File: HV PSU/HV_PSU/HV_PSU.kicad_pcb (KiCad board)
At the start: 2 copper layers, 106 parts, among them J1 Screw_Terminal_01x07, J10 MountingHole_Pad, J11 MountingHole_Pad, J12 MountingHole_Pad, J13 MountingHole_Pad, J2 MountingHole_Pad, J3 MountingHole_Pad, J4 MountingHole_Pad, J5 MountingHole_Pad, J6 MountingHole_Pad, J7 MountingHole_Pad, J8 MountingHole_Pad, J9 MountingHole_Pad, Q1 2N7002, Q2 IRFS4227, Q3 IRFS4227, U1 L7812, U2 TPS2814D

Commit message: backup
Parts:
- C10, C11, C12, C13, C6, C7, C8, C9: footprint Capacitor_THT:C_Disc_D16.0mm_W5.0mm_P10.00mm -> HV_caps:HVC-30KV-D17-F12.5-102K
- D1, D2: value UF4007 -> 1N4148WS; footprint Diode_THT:D_DO-41_SOD81_P10.16mm_Horizontal -> Diode_SMD:D_SOD-323
- D20, D21, D22, D23: value UF4007 -> ES1J; footprint Diode_THT:D_DO-41_SOD81_P10.16mm_Horizontal -> Diode_SMD:D_SMA-SMB_Universal_Handsoldering
- moved D4 175.6 mm to (120.5, 156.8)
- moved D5 175.6 mm to (139.7, 152.4)
- moved D7 158.9 mm to (129.5, 180.3)
- moved D6 158.9 mm to (149.1, 170.8)
- moved D8 153.4 mm to (180.0, 170.3), turned to 90 degrees
- moved J2 133.3 mm to (219.7, 87.6)
- moved D9 115.4 mm to (185.4, 170.2), turned to 90 degrees
- moved D15 107.1 mm to (227.3, 168.9), turned to 90 degrees
- moved C8 103.3 mm to (268.1, 85.1)
- moved R11 101.9 mm to (172.7, 129.5)
- moved D10 101.8 mm to (194.3, 170.2), turned to 90 degrees
- moved J4 101.6 mm to (233.7, 180.3)
- moved J3 101.2 mm to (233.7, 147.3)
- moved C10 100.0 mm to (280.8, 91.4)
- moved D13 96.8 mm to (209.6, 171.4), turned to 90 degrees
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
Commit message: Some PCB placement
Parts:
- moved D4 147.6 mm to (254.5, 95.0), turned to -90 degrees
- moved D7 140.2 mm to (264.8, 143.4), turned to 90 degrees
- moved D6 130.0 mm to (264.1, 110.2), turned to 90 degrees
- moved D8 120.2 mm to (273.7, 95.0), turned to -90 degrees
- moved D5 117.5 mm to (254.6, 128.1), turned to -90 degrees
- moved D12 108.8 mm to (292.8, 95.0), turned to -90 degrees
- moved D10 107.3 mm to (283.2, 110.2)
- moved D16 101.9 mm to (312.0, 95.0), turned to -90 degrees
- moved D9 99.0 mm to (275.0, 128.1), turned to -90 degrees
- moved D13 96.2 mm to (295.4, 128.1), turned to -90 degrees
- moved R12 93.8 mm to (265.3, 120.8), turned to 90 degrees
- moved R10 93.1 mm to (265.3, 114.4), turned to 90 degrees
- moved R32 93.0 mm to (313.3, 120.8), turned to 90 degrees
- moved R30 92.8 mm to (313.3, 114.4), turned to 90 degrees
- moved R36 92.0 mm to (322.8, 120.8), turned to 90 degrees
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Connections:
- D10 pad 1: Net-(D10-Pad1) -> Net-(R18-Pad2)
- D10 pad 2: Net-(D10-Pad2) -> Net-(C10-Pad1)
- D11 pad 2: Net-(D10-Pad1) -> Net-(D11-Pad2)
- D12 pad 1: Net-(D12-Pad1) -> Net-(C10-Pad2)
- D12 pad 2: Net-(D12-Pad2) -> Net-(R22-Pad2)
- D13 pad 1: Net-(D12-Pad2) -> Net-(D13-Pad1)
- D14 pad 1: Net-(D14-Pad1) -> Net-(R26-Pad2)
- D14 pad 2: Net-(D14-Pad2) -> Net-(C10-Pad2)
- D15 pad 2: Net-(D14-Pad1) -> Net-(D15-Pad2)
- D16 pad 1: Net-(D16-Pad1) -> Net-(C12-Pad2)
- D17 pad 1: Net-(D16-Pad2) -> Net-(D17-Pad1)
- D18 pad 1: Net-(D18-Pad1) -> Net-(R34-Pad2)
- D18 pad 2: Net-(D18-Pad2) -> Net-(C12-Pad2)
- D19 pad 2: Net-(D18-Pad1) -> Net-(R37-Pad1)
- D4 pad 1: Net-(D4-Pad1) -> Net-(C6-Pad2)
- D4 pad 2: Net-(D4-Pad2) -> Net-(R6-Pad2)
- D5 pad 1: Net-(D4-Pad2) -> Net-(D5-Pad1)
- D6 pad 2: Net-(D6-Pad2) -> Net-(C6-Pad2)
- D7 pad 2: Net-(D6-Pad1) -> Net-(D7-Pad2)
- D8 pad 1: Net-(D8-Pad1) -> Net-(C10-Pad1)
- D8 pad 2: Net-(D8-Pad2) -> Net-(R14-Pad2)
- D9 pad 1: Net-(D8-Pad2) -> Net-(D9-Pad1)
- R10 pad 2: Net-(C6-Pad2) -> Net-(D6-Pad1)
- R13 pad 1: Net-(D6-Pad2) -> Net-(D7-Pad2)
- R14 pad 2: Net-(C10-Pad1) -> Net-(R14-Pad2)
- R17 pad 1: Net-(D8-Pad1) -> Net-(D9-Pad1)
- R18 pad 2: Net-(C10-Pad1) -> Net-(R18-Pad2)
- R21 pad 1: Net-(D10-Pad2) -> Net-(D11-Pad2)
- R22 pad 2: Net-(C10-Pad2) -> Net-(R22-Pad2)
- R25 pad 1: Net-(D12-Pad1) -> Net-(D13-Pad1)
- R26 pad 2: Net-(C10-Pad2) -> Net-(R26-Pad2)
- R29 pad 1: Net-(D14-Pad2) -> Net-(D15-Pad2)
- R30 pad 2: Net-(C12-Pad2) -> Net-(D16-Pad2)
- R33 pad 1: Net-(D16-Pad1) -> Net-(D17-Pad1)
- R34 pad 2: Net-(C12-Pad2) -> Net-(R34-Pad2)
- R37 pad 1: Net-(D18-Pad2) -> Net-(R37-Pad1)
- R6 pad 2: Net-(C6-Pad2) -> Net-(R6-Pad2)
- R9 pad 1: Net-(D4-Pad1) -> Net-(D5-Pad1)

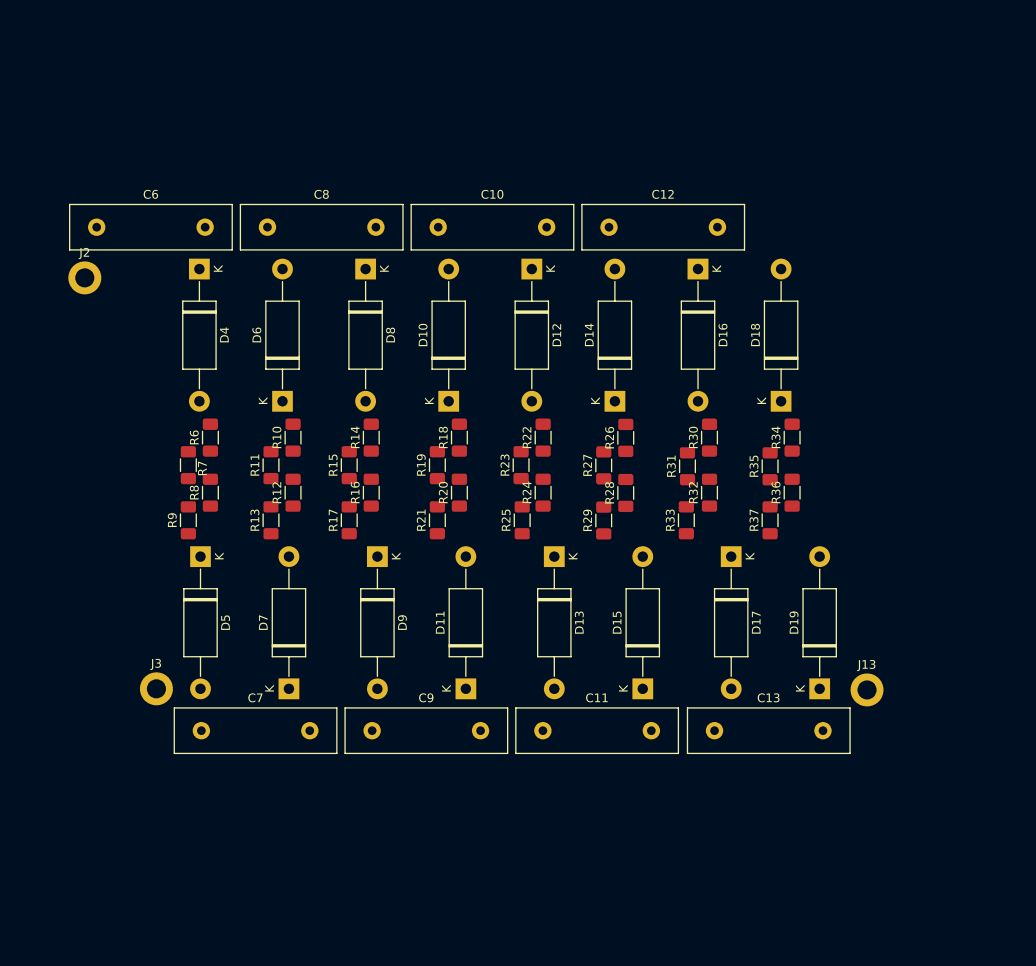
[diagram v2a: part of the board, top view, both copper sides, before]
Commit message: Tilted caps
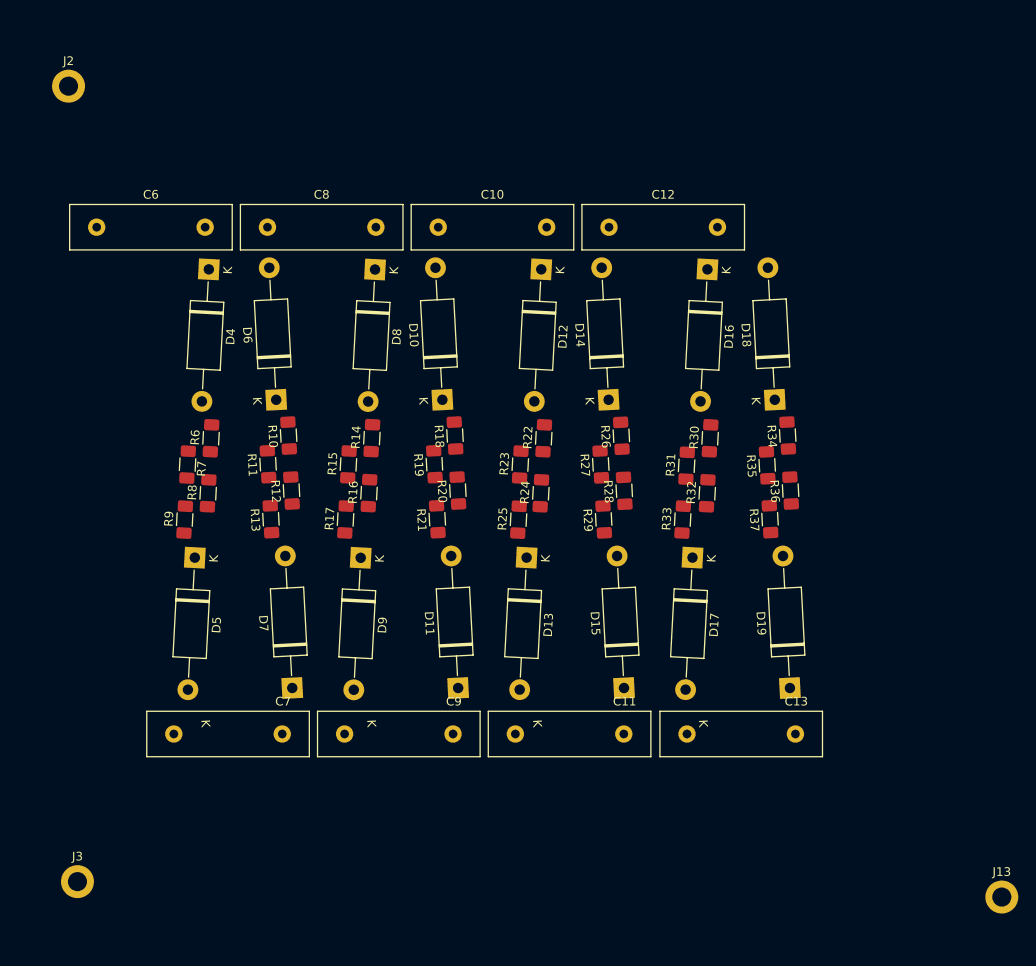
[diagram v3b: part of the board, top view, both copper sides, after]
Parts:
- moved J13 28.5 mm to (347.0, 167.4)
- moved J3 24.0 mm to (240.5, 165.6)
- moved J2 22.2 mm to (239.4, 73.9)
- moved D17 4.46 mm to (311.3, 128.3), turned to -93 degrees
- moved D19 3.43 mm to (322.6, 143.3), turned to 93 degrees
- moved C11 3.20 mm to (290.9, 148.6)
- moved C13 3.20 mm to (310.7, 148.6)
- moved C7 3.20 mm to (251.6, 148.6)
- moved C9 3.20 mm to (271.2, 148.6)
- moved D13 3.20 mm to (292.2, 128.3), turned to -93 degrees
- moved D15 2.16 mm to (303.5, 143.3), turned to 93 degrees
- moved D9 1.93 mm to (273.1, 128.3), turned to -93 degrees
- moved D8 1.09 mm to (274.8, 95.0), turned to -93 degrees
- moved D16 1.09 mm to (313.1, 95.0), turned to -93 degrees
- moved D4 1.09 mm to (255.6, 95.0), turned to -93 degrees
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
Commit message: Initial placement
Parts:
- D21, D22: value ES1J -> 1N4148WS; footprint Diode_SMD:D_SMA-SMB_Universal_Handsoldering -> Diode_SMD:D_SOD-323
- moved C14 229.1 mm to (103.0, 28.1), turned to -90 degrees
- moved C17 225.0 mm to (96.5, 28.1), turned to -90 degrees
- moved C18 221.6 mm to (89.9, 28.1), turned to -90 degrees
- moved C16 219.0 mm to (83.4, 28.1), turned to -90 degrees
- moved C15 217.3 mm to (76.9, 28.0), turned to -90 degrees
- moved D24 215.0 mm to (51.1, 30.4)
- moved J9 212.1 mm to (114.3, 22.4)
- moved J5 210.1 mm to (109.2, 22.4)
- moved D21 206.8 mm to (52.1, 22.8), turned to 180 degrees
- moved J11 206.6 mm to (114.3, 37.6)
- moved D20 205.8 mm to (43.3, 26.6), turned to 180 degrees
- moved D25 202.2 mm to (51.4, 45.7)
- moved J7 193.7 mm to (114.3, 32.5)
- moved R38 193.1 mm to (52.0, 25.4), turned to 180 degrees
- moved L1 190.5 mm to (95.4, 70.7), turned to 180 degrees
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
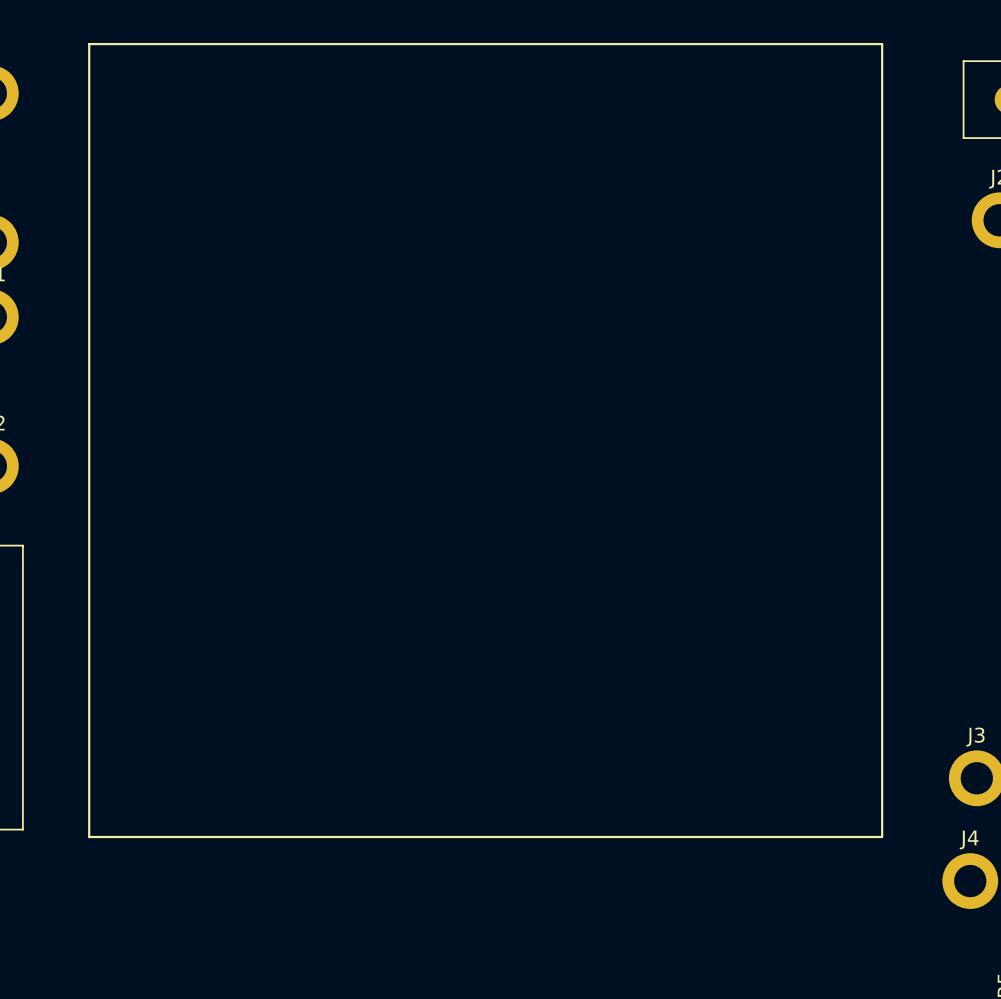
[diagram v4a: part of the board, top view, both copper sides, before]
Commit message: Added transformer footprint, model and symbol
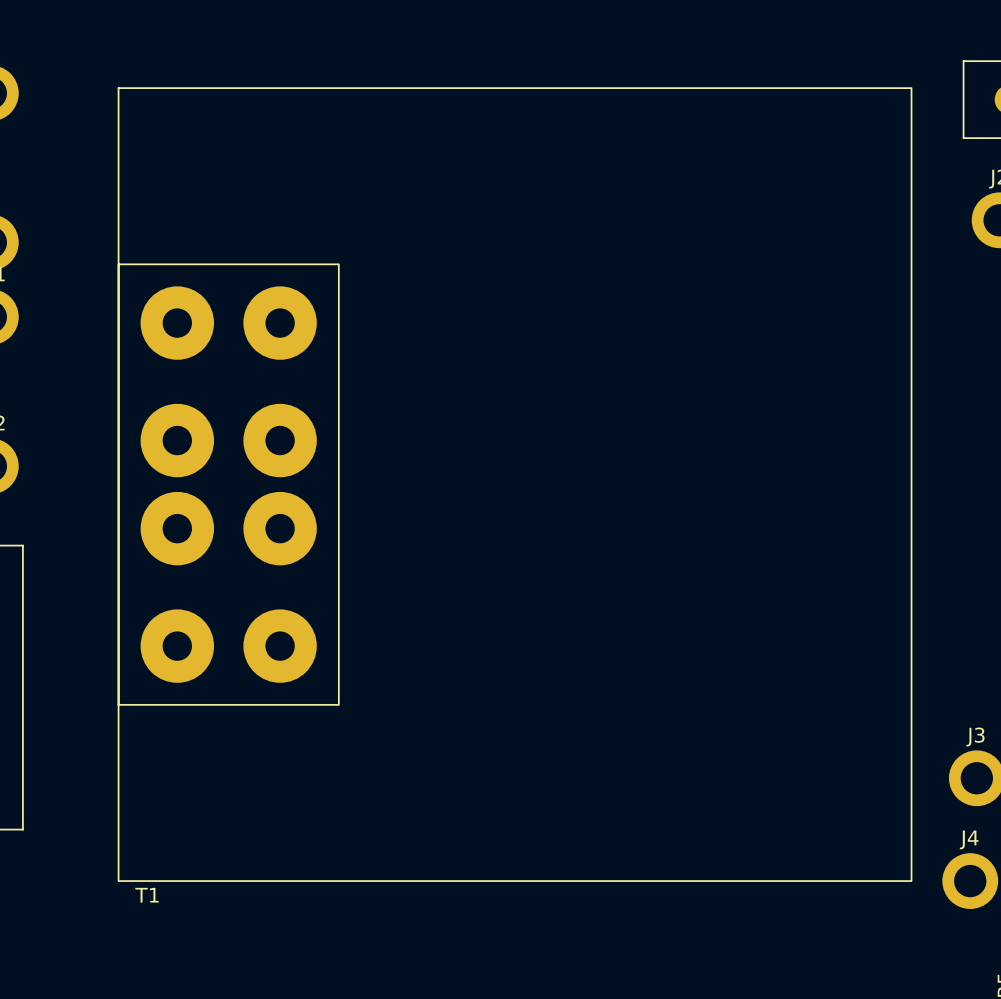
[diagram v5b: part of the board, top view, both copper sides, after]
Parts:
- added T1: UY12, HV_xformer:UY12, F.Cu at (150.0, 49.0)
- J2: value MountingHole_Pad -> AC_HV_1
- J3: value MountingHole_Pad -> AC_HV_2
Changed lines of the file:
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@@
     )
   )
+  (footprint "HV_xformer:UY12" (layer "F.Cu")
+    (at 150 49)
+    (property "Sheetfile" "HV_PSU.kicad_sch")
+    (property "Sheetname" "")
+    (attr smd)
+    (fp_text reference "T1" (at -25 28 unlocked) (layer "F.SilkS")
+      (effects (font (size 1 1) (thickness 0.15)))
+    )
+    (fp_text value "UY12" (at 0 1 unlocked) (layer "F.Fab")
+      (effects (font (size 1 1) (thickness 0.15)))
+    )
+    (fp_rect (start -27 -27) (end 27 27) (layer "F.SilkS") (width 0.12) (fill none))
+    (fp_rect (start -27 15) (end -12 -15) (layer "F.SilkS") (width 0.12) (fill none))
+    (pad "1" thru_hole circle (at -16 -11) (size 5 5) (drill 2) (layers *.Cu *.Mask)
+      (net 15 "/T_A") (pinfunction "1") (pintype "passive"))
+    (pad "1" thru_hole circle (at -23 -11) (size 5 5) (drill 2) (layers *.Cu *.Mask)
+      (net 15 "/T_A") (pinfunction "1") (pintype "passive"))
+    (pad "2" thru_hole circle (at -16 -3) (size 5 5) (drill 2) (layers *.Cu *.Mask)
+      (net 23 "/T_TAP") (pinfunction "2") (pintype "passive"))
+    (pad "2" thru_hole circle (at -23 -3) (size 5 5) (drill 2) (layers *.Cu *.Mask)
+      (net 23 "/T_TAP") (pinfunction "2") (pintype "passive"))
+    (pad "3" thru_hole circle (at -23 3) (size 5 5) (drill 2) (layers *.Cu *.Mask)
+      (net 23 "/T_TAP") (pinfunction "3") (pintype "passive"))
+    (pad "3" thru_hole circle (at -16 3) (size 5 5) (drill 2) (layers *.Cu *.Mask)
+      (net 23 "/T_TAP") (pinfunction "3") (pintype "passive"))
+    (pad "4" thru_hole circle (at -23 11) (size 5 5) (drill 2) (layers *.Cu *.Mask)
+      (net 16 "/T_B") (pinfunction "4") (pintype "passive"))
+    (pad "4" thru_hole circle (at -16 11) (size 5 5) (drill 2) (layers *.Cu *.Mask)
+      (net 16 "/T_B") (pinfunction "4") (pintype "passive"))
+    (model "${KIPRJMOD}/models/UY12.step"
+      (offset (xyz -27 27 0))
+      (scale (xyz 1 1 1))
+      (rotate (xyz 0 0 90))
+    )
+  )
   (footprint "Capacitor_THT:C_Rect_L18.0mm_W5.0mm_P15.00mm_FKS3_FKP3" (layer "F.Cu")
     (at 89.936 28.15 -90)
@@
       (effects (font (size 1 1) (thickness 0.15)))
     )
-    (fp_text value "MountingHole_Pad" (at 0 2.9) (layer "F.Fab") hide
+    (fp_text value "AC_HV_1" (at 0 2.9) (layer "F.Fab") hide
       (effects (font (size 1 1) (thickness 0.15)))
     )
@@
       (effects (font (size 1 1) (thickness 0.15)))
     )
-    (fp_text value "MountingHole_Pad" (at 0 2.9) (layer "F.Fab") hide
+    (fp_text value "AC_HV_2" (at 0 2.9) (layer "F.Fab") hide
       (effects (font (size 1 1) (thickness 0.15)))
     )
@@
     )
   )
-  (gr_rect (start 121 19) (end 175 73) (layer "F.SilkS") (width 0.15) (fill none))
 )

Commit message: Rearranging layout
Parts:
- removed J10, J11, J12, J6, J7, J8, J9: MountingHole_Pad, MountingHole:MountingHole_2.2mm_M2_DIN965_Pad
- added H1: MountingHole_Pad, MountingHole:MountingHole_3.2mm_M3_Pad_Via, F.Cu at (6.00, 7.00)
- added H2: MountingHole_Pad, MountingHole:MountingHole_3.2mm_M3_Pad_Via, F.Cu at (7.00, 87.0)
- added H3: MountingHole_Pad, MountingHole:MountingHole_3.2mm_M3_Pad_Via, F.Cu at (108.0, 85.0)
- added H4: MountingHole_Pad, MountingHole:MountingHole_3.2mm_M3_Pad_Via, F.Cu at (96.0, 6.00)
- added R44: 0, Resistor_SMD:R_0603_1608Metric_Pad0.98x0.95mm_HandSolder, F.Cu at (106.0, 80.0)
- J5: value MountingHole_Pad -> AC_HV_2
- moved D3 83.8 mm to (104.5, 71.0), turned to 90 degrees
- moved R5 82.1 mm to (104.5, 66.0)
- moved J13 80.0 mm to (191.0, 80.0)
- moved T1 75.1 mm to (76.0, 62.0), turned to -90 degrees
- moved C11 74.3 mm to (158.0, 74.0)
- moved C12 74.3 mm to (168.8, 15.6)
- moved C13 74.3 mm to (177.8, 74.0)
- moved C7 74.3 mm to (118.6, 74.0)
- moved C9 74.3 mm to (138.3, 74.0)
- moved D10 74.3 mm to (149.6, 35.5)
- moved D12 74.3 mm to (161.0, 20.4)
- moved D13 74.3 mm to (159.3, 53.7)
- moved D15 74.3 mm to (170.5, 68.7)
- moved D16 74.3 mm to (180.1, 20.4)
- moved D17 74.3 mm to (178.4, 53.7)
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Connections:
- J5 pad 1: /T_A -> Net-(C7-Pad1)

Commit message: More re-arranging
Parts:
- removed H4: MountingHole_Pad, MountingHole:MountingHole_3.2mm_M3_Pad_Via
- D1, D2, D21, D22: value 1N4148WS -> 1N4148W; footprint Diode_SMD:D_SOD-323 -> Diode_SMD:D_SOD-123
- moved C15 62.7 mm to (13.8, 41.5)
- moved C16 62.6 mm to (20.4, 41.5)
- moved C18 62.6 mm to (26.9, 41.5)
- moved C14 62.6 mm to (40.0, 41.5)
- moved C17 62.6 mm to (33.5, 41.5)
- moved D25 50.4 mm to (13.2, 67.6)
- moved R41 50.4 mm to (13.2, 70.2)
- moved D22 50.4 mm to (14.3, 60.0)
- moved R39 50.4 mm to (14.2, 62.5)
- moved R43 50.4 mm to (9.00, 70.2)
- moved U1 50.3 mm to (15.8, 88.0), turned to -90 degrees
- moved Q3 50.0 mm to (25.9, 64.5)
- moved D23 49.0 mm to (29.9, 73.0)
- moved L1 48.7 mm to (68.0, 95.9), turned to 180 degrees
- moved J1 45.9 mm to (5.00, 56.5)
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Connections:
- D2 pad 1: Net-(D2-Pad1) -> Net-(R43-Pad1)
- D20 pad 1: Net-(D20-Pad1) -> /T_A
- D20 pad 2: Net-(D1-Pad1) -> Net-(R42-Pad2)
- D23 pad 1: Net-(D23-Pad1) -> /T_B
- D23 pad 2: Net-(D2-Pad1) -> Net-(D23-Pad2)
- Q1 pad 1: Net-(D2-Pad1) -> Net-(R43-Pad1)
- R4 pad 1: Net-(D2-Pad1) -> Net-(R43-Pad1)
- R42 pad 1: Net-(D20-Pad1) -> Net-(D1-Pad1)
- R42 pad 2: /T_A -> Net-(R42-Pad2)
- R43 pad 1: Net-(D23-Pad1) -> Net-(R43-Pad1)
- R43 pad 2: /T_B -> Net-(D23-Pad2)
- U2 pad 1: Net-(D2-Pad1) -> Net-(R43-Pad1)
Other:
- board outline added: 200 x 80 mm

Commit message: backup
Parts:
- C14, C17, C18: footprint Capacitor_THT:C_Rect_L18.0mm_W5.0mm_P15.00mm_FKS3_FKP3 -> Capacitor_THT:C_Rect_L18.0mm_W9.0mm_P15.00mm_FKS3_FKP3
- C15, C16: footprint Capacitor_THT:C_Rect_L18.0mm_W5.0mm_P15.00mm_FKS3_FKP3 -> Capacitor_THT:C_Rect_L18.0mm_W9.0mm_P15.00mm_FKS3_FKP3; moved to B.Cu
- D24, D25: value BZV55B15 -> PJSD12W; footprint Diode_SMD:D_MiniMELF -> Diode_SMD:D_SOD-323_HandSoldering
- D3: value BZV55B15 -> DZ2S150X0L; footprint Diode_SMD:D_MiniMELF -> Diode_SMD:D_SOD-523
- moved U2 17.6 mm to (7.00, 32.0), turned to 90 degrees
- moved C5 15.3 mm to (2.98, 31.0), turned to 90 degrees
- moved R3 14.3 mm to (-3.14, 30.5), turned to -90 degrees
- moved C16 13.1 mm to (33.5, 41.5)
- moved C18 9.90 mm to (17.0, 41.5)
- moved R1 8.71 mm to (-5.56, 35.5), turned to -90 degrees
- moved Q1 8.68 mm to (1.36, 35.5), turned to 90 degrees
- moved C15 8.66 mm to (22.5, 41.5)
- moved C3 7.31 mm to (-3.02, 35.5), turned to -90 degrees
- moved C17 5.45 mm to (28.0, 41.5)
- moved D25 2.73 mm to (14.0, 65.0)
- moved D24 2.69 mm to (13.5, 34.0)
- moved C14 1.00 mm to (39.0, 41.5)
- moved D3 0.50 mm to (93.0, 83.5)
